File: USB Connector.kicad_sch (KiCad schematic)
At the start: 18 parts, among them P1 USB_C_Plug_USB2.0, U1 CH330N, U5 WE-TVS-82400102

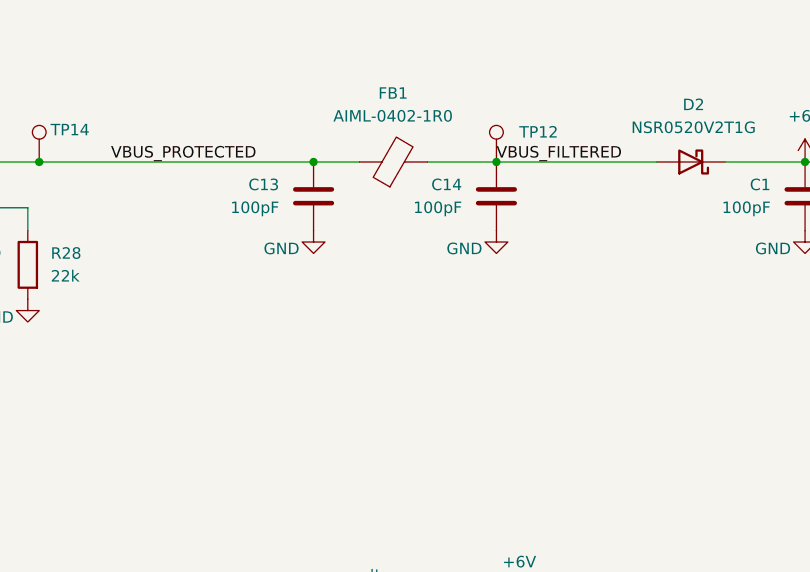
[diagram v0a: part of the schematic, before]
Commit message: Fixing filter response to put loads at 10 MHz signals and 1 GHz signals (low pass RC and ferrite) at DC power supply (rejecting high frequency noise in the power supply).
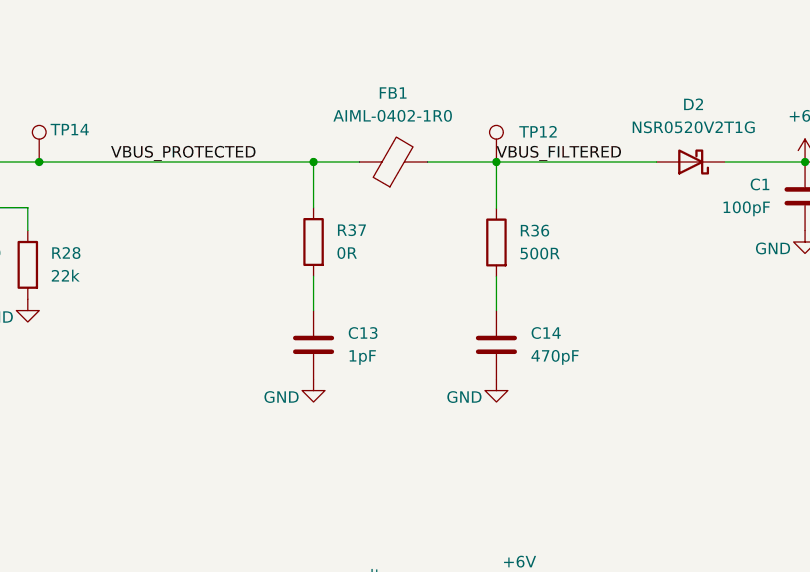
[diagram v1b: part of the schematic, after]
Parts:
- added R36: 500R, Resistor_SMD:R_0402_1005Metric, symbol Device:R
- added R37: 0R, Resistor_SMD:R_0402_1005Metric, symbol Device:R
- C13: value 100pF -> 1pF
- C14: value 100pF -> 470pF
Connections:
- net VBUS_FILTERED: now also R36.1; no longer C14.1
- net VBUS_PROTECTED: now also R37.1; no longer C13.1
- new net: C14.1, R36.2
- new net: C13.1, R37.2
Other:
- moved on the sheet: C13, C14

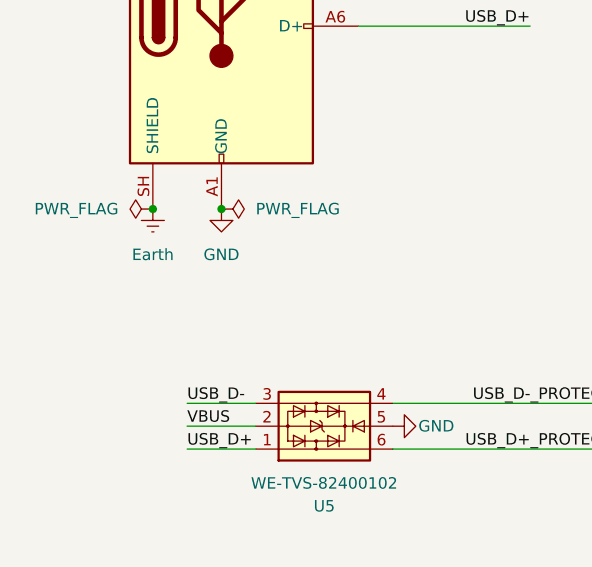
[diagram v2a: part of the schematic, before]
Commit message: Adding resistance and capacitance connecting GND and Earth in the peripheral device
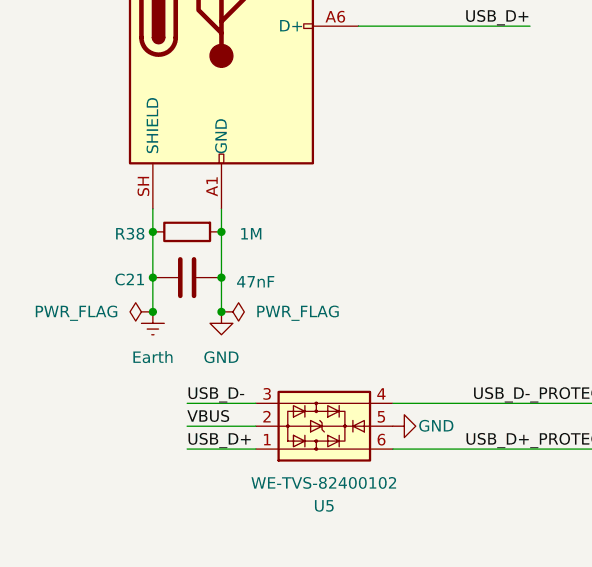
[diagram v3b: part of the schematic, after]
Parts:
- added C21: 47nF, Capacitor_SMD:C_0402_1005Metric, symbol Device:C
- added R38: 1M, Resistor_SMD:R_0402_1005Metric, symbol Device:R
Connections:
- net Earth: now also C21.1, R38.1
- net GND: now also C21.2, R38.2
